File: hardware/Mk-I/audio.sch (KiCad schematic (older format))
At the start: 10 parts, among them U1 AP7313-18SRG-7, U5 SGTL5000XNAA3R2

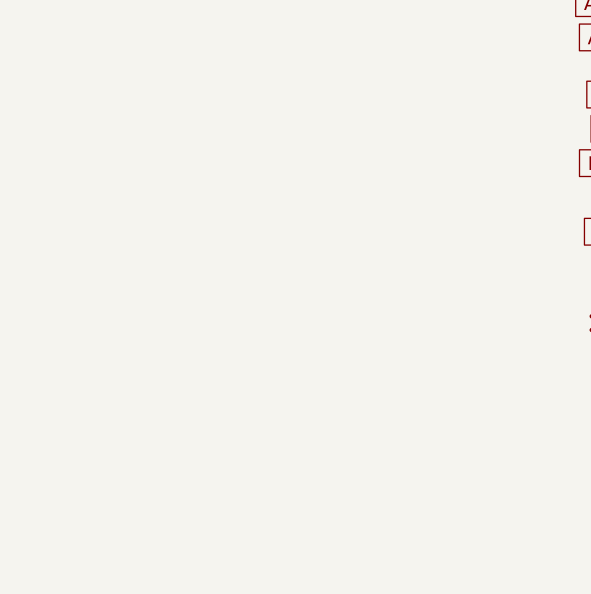
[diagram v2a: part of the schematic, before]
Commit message: HW: Change 3.5 socket and put them on top
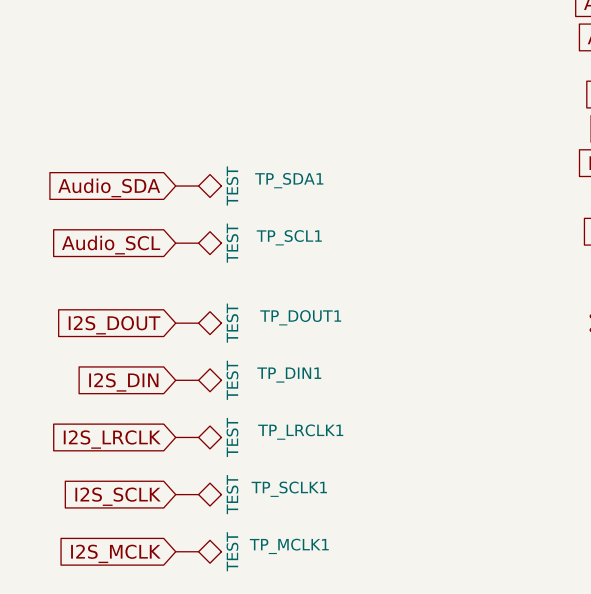
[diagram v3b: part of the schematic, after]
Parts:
- added TP_DIN1, TP_DOUT1, TP_LRCLK1, TP_MCLK1, TP_SCL1, TP_SCLK1, TP_SDA1: TEST, Measurement_Points:Measurement_Point_Round-SMD-Pad_Small, symbol TEST
- HP_OUT1, LINE_IN1: value 1503 02 -> SJ-3523-SMT; footprint POSS:lumberg_3.5_audio_jack_1503_02 -> POSS:SJ-3523-SMT
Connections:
- net Audio_SCL: now also TP_SCL1.1
- net Audio_SDA: now also TP_SDA1.1
- net I2S_DIN: now also TP_DIN1.1
- net I2S_DOUT: now also TP_DOUT1.1
- net I2S_LRCLK: now also TP_LRCLK1.1
- net I2S_MCLK: now also TP_MCLK1.1
- net I2S_SCLK: now also TP_SCLK1.1
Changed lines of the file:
@@
 P 7100 4425
 F 0 "HP_OUT1" H 7175 3800 60  0000 C CNN
-F 1 "1503 02" H 7100 4425 60  0001 C CNN
-F 2 "POSS:lumberg_3.5_audio_jack_1503_02" H 7100 4425 60  0001 C CNN
+F 1 "SJ-3523-SMT" H 7100 4425 60  0001 C CNN
+F 2 "POSS:SJ-3523-SMT" H 7100 4425 60  0001 C CNN
 F 3 "" H 7100 4425 60  0001 C CNN
 	1    7100 4425
@@
 P 7100 3825
 F 0 "LINE_IN1" H 7175 3200 60  0000 C CNN
-F 1 "1503 02" H 6950 3200 60  0001 C CNN
-F 2 "POSS:lumberg_3.5_audio_jack_1503_02" H 7100 3825 60  0001 C CNN
+F 1 "SJ-3523-SMT" H 6950 3200 60  0001 C CNN
+F 2 "POSS:SJ-3523-SMT" H 7100 3825 60  0001 C CNN
 F 3 "" H 7100 3825 60  0001 C CNN
 	1    7100 3825
@@
 	4800 2300 4800 2250
 Connection ~ 4800 2250
+$Comp
+L TEST TP_MCLK1
+U 1 1 59ECF1C0
+P 2200 5700
+F 0 "TP_MCLK1" V 2200 6200 50  0000 C BNN
+F 1 "TEST" H 2200 5950 50  0000 C CNN
+F 2 "Measurement_Points:Measurement_Point_Round-SMD-Pad_Small" H 2200 5700 50  0001 C CNN
+F 3 "" H 2200 5700 50  0001 C CNN
+	1    2200 5700
+	0    1    1    0
+$EndComp
+Text GLabel 2200 5700 0    60   Input ~ 0
+I2S_MCLK
+Text GLabel 2200 5450 0    60   Input ~ 0
+I2S_SCLK
+Text GLabel 2200 5200 0    60   Input ~ 0
+I2S_LRCLK
+Text GLabel 2200 4950 0    60   Input ~ 0
+I2S_DIN
+Text GLabel 2200 4700 0    60   Input ~ 0
+I2S_DOUT
+$Comp
+L TEST TP_SCLK1
+U 1 1 59ECF440
+P 2200 5450
+F 0 "TP_SCLK1" V 2200 5950 50  0000 C BNN
+F 1 "TEST" H 2200 5700 50  0000 C CNN
+F 2 "Measurement_Points:Measurement_Point_Round-SMD-Pad_Small" H 2200 5450 50  0001 C CNN
+F 3 "" H 2200 5450 50  0001 C CNN
+	1    2200 5450
+	0    1    1    0
+$EndComp
+$Comp
+L TEST TP_LRCLK1
+U 1 1 59ECF47A
+P 2200 5200
+F 0 "TP_LRCLK1" V 2200 5750 50  0000 C BNN
+F 1 "TEST" H 2200 5450 50  0000 C CNN
+F 2 "Measurement_Points:Measurement_Point_Round-SMD-Pad_Small" H 2200 5200 50  0001 C CNN
+F 3 "" H 2200 5200 50  0001 C CNN
+	1    2200 5200
+	0    1    1    0
+$EndComp
+$Comp
+L TEST TP_DIN1
+U 1 1 59ECF4B7
+P 2200 4950
+F 0 "TP_DIN1" V 2200 5450 50  0000 C BNN
+F 1 "TEST" H 2200 5200 50  0000 C CNN
+F 2 "Measurement_Points:Measurement_Point_Round-SMD-Pad_Small" H 2200 4950 50  0001 C CNN
+F 3 "" H 2200 4950 50  0001 C CNN
+	1    2200 4950
+	0    1    1    0
+$EndComp
+$Comp
+L TEST TP_DOUT1
+U 1 1 59ECF4F7
+P 2200 4700
+F 0 "TP_DOUT1" V 2200 5250 50  0000 C BNN
+F 1 "TEST" H 2200 4950 50  0000 C CNN
+F 2 "Measurement_Points:Measurement_Point_Round-SMD-Pad_Small" H 2200 4700 50  0001 C CNN
+F 3 "" H 2200 4700 50  0001 C CNN
+	1    2200 4700
+	0    1    1    0
+$EndComp
+Text GLabel 2200 4350 0    60   Input ~ 0
+Audio_SCL
+Text GLabel 2200 4100 0    60   Input ~ 0
+Audio_SDA
+$Comp
+L TEST TP_SCL1
+U 1 1 59ECF77C
+P 2200 4350
+F 0 "TP_SCL1" V 2200 4850 50  0000 C BNN
+F 1 "TEST" H 2200 4600 50  0000 C CNN
+F 2 "Measurement_Points:Measurement_Point_Round-SMD-Pad_Small" H 2200 4350 50  0001 C CNN
+F 3 "" H 2200 4350 50  0001 C CNN
+	1    2200 4350
+	0    1    1    0
+$EndComp
+$Comp
+L TEST TP_SDA1
+U 1 1 59ECF7C8
+P 2200 4100
+F 0 "TP_SDA1" V 2200 4600 50  0000 C BNN
+F 1 "TEST" H 2200 4350 50  0000 C CNN
+F 2 "Measurement_Points:Measurement_Point_Round-SMD-Pad_Small" H 2200 4100 50  0001 C CNN
+F 3 "" H 2200 4100 50  0001 C CNN
+	1    2200 4100
+	0    1    1    0
+$EndComp
 $EndSCHEMATC
